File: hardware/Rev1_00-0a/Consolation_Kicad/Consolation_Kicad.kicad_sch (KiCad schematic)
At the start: 17 parts

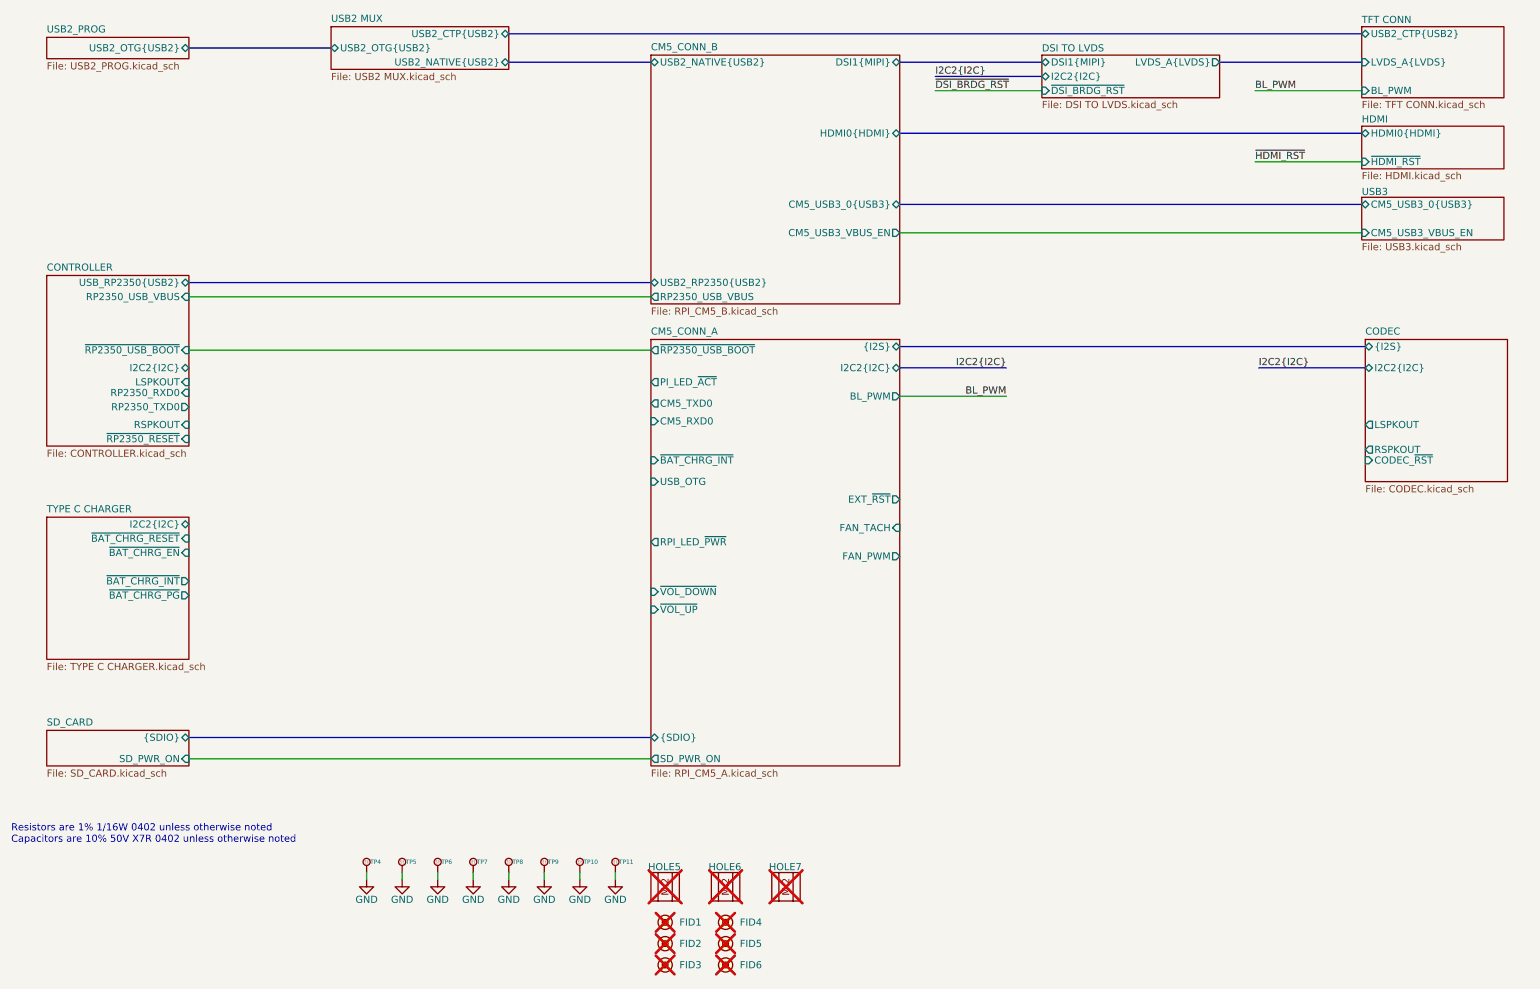
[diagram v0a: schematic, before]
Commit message: Major update to consolation schematics to include - Power supply - RESET SUPERVISOR - Review of GPIO and pinmux
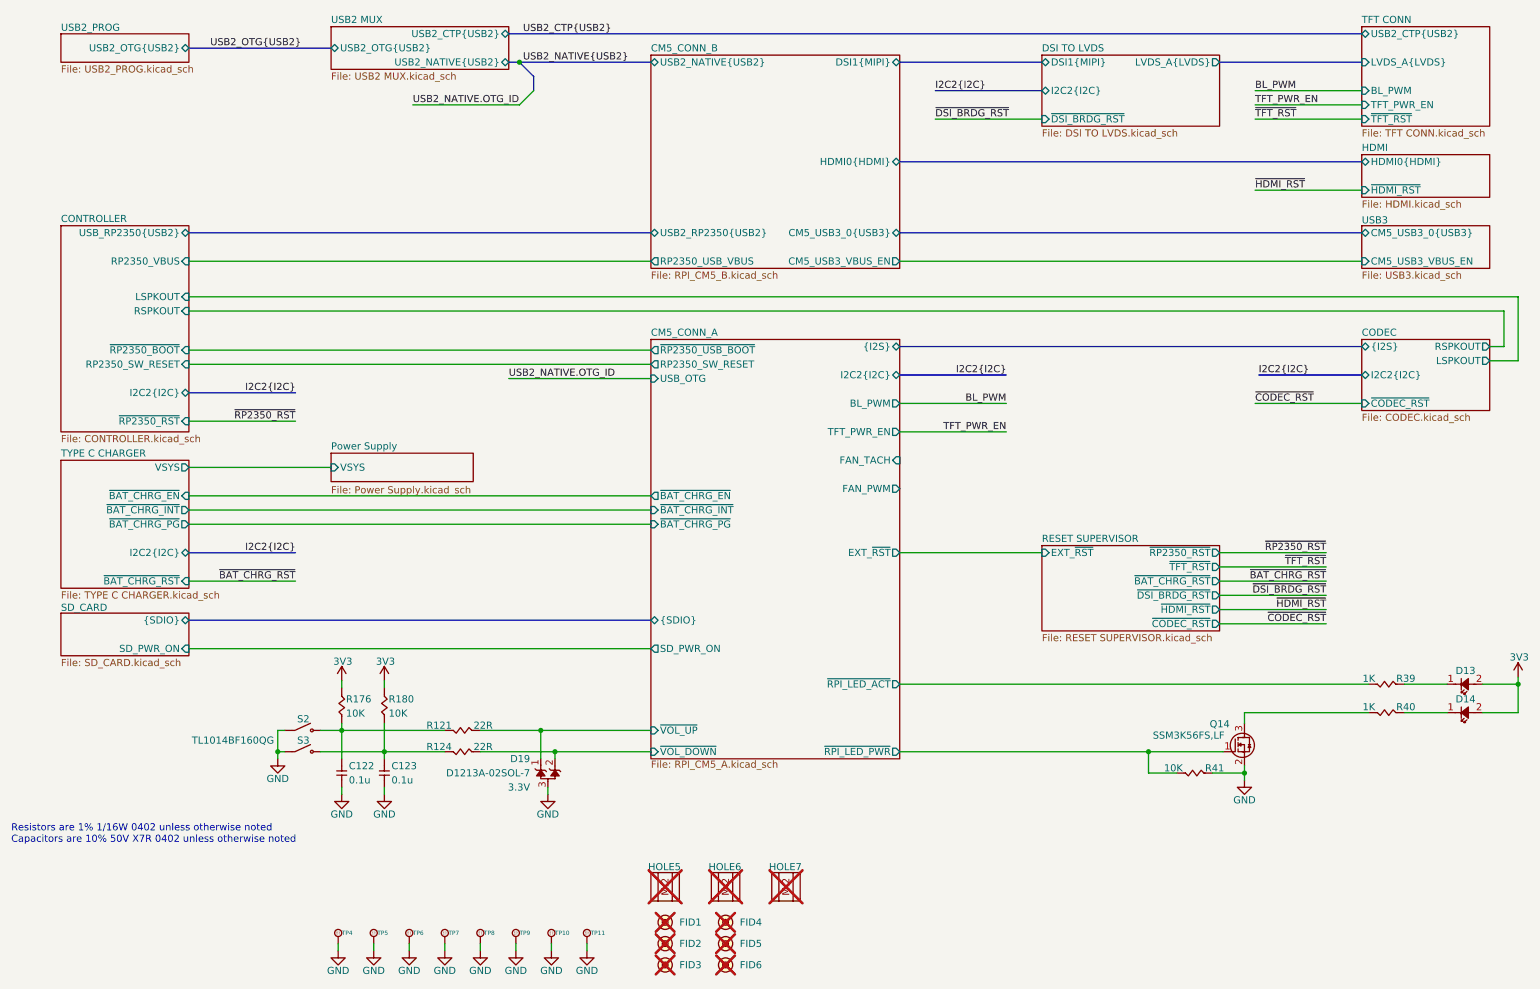
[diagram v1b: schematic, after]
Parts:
- added C122, C123: 0.1u, footprint:CAP_NONPOL_0402, symbol KicadCompDb:Capacitors/CAP_CER_SMT_00001
- added D13, D14: LTST-C190KGKT, footprint:LED_0603, symbol KicadCompDb:Diodes/DIODE_00007
- added D19: D1213A-02SOL-7, footprint:SOT-23-3, symbol KicadCompDb:ESD Diodes/ESD_DIODE_00002
- added Q14: SSM3K56FS,LF, footprint:SC-75, symbol KicadCompDb:Mosfet/MOSFET_00002
- added R121, R124: 22R, footprint:RES_0402, symbol KicadCompDb:Resistors/RES_SMT_00015
- added R176, R180, R41: 10K, footprint:RES_0402, symbol KicadCompDb:Resistors/RES_SMT_00013
- added R39, R40: 1K, footprint:RES_0402, symbol KicadCompDb:Resistors/RES_SMT_00004
- added S2, S3: TL1014BF160QG, footprint:TL1014B, symbol KicadCompDb:Miscellaneous/MISC_00016
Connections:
- net CM5_CONN_A/~{VOL_DOWN}: now also D19.2 (A), R124.1
- net CM5_CONN_A/~{VOL_UP}: now also D19.1, R121.1
- net GND: now also C122.1, C123.1, D19.3 (GND), Q14.2 (S), R41.2, S2.1, S3.1
- new net: C122.2, R121.2, R176.1, S2.2
- new net: Q14.3 (D), R40.2
- new net: D14.1 (K), R40.1
- new net: C123.2, R124.2, R180.1, S3.2
- new net: D13.1 (K), R39.1
- new net 3V3: D13.2 (A), D14.2 (A), R176.2, R180.2
- new net CM5_CONN_A/~{RPI_LED_ACT}: R39.2
- new net CM5_CONN_A/~{RPI_LED_PWR}: Q14.1 (G), R41.1
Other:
- added sheet Power Supply (Power Supply.kicad_sch)
- added sheet RESET SUPERVISOR (RESET SUPERVISOR.kicad_sch)
- sheet CM5_CONN_A ports: added RP2350_SW_RESET, TFT_PWR_EN, ~{BAT_CHRG_EN}, ~{BAT_CHRG_PG}, ~{RPI_LED_ACT}, ~{RPI_LED_PWR}; removed CM5_RXD0, CM5_TXD0, PI_LED_~{ACT}, RPI_LED_~{PWR}
- sheet CODEC ports: added ~{CODEC_RST}; removed CODEC_~{RST}
- sheet CONTROLLER ports: added RP2350_SW_RESET, RP2350_VBUS, ~{RP2350_BOOT}, ~{RP2350_RST}; removed RP2350_RXD0, RP2350_TXD0, RP2350_USB_VBUS, ~{RP2350_RESET}, ~{RP2350_USB_BOOT}
- sheet TFT CONN ports: added TFT_PWR_EN, ~{TFT_RST}; removed none
- sheet TYPE C CHARGER ports: added VSYS, ~{BAT_CHRG_RST}; removed ~{BAT_CHRG_RESET}
- moved on the sheet: TP10, TP11, TP4, TP5, TP6, TP7, TP8, TP9

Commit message: Removed unnecessary functions (USB2 mux, CapTouch) Adjusted 220uF alum capacitor for codec (slimmer version)
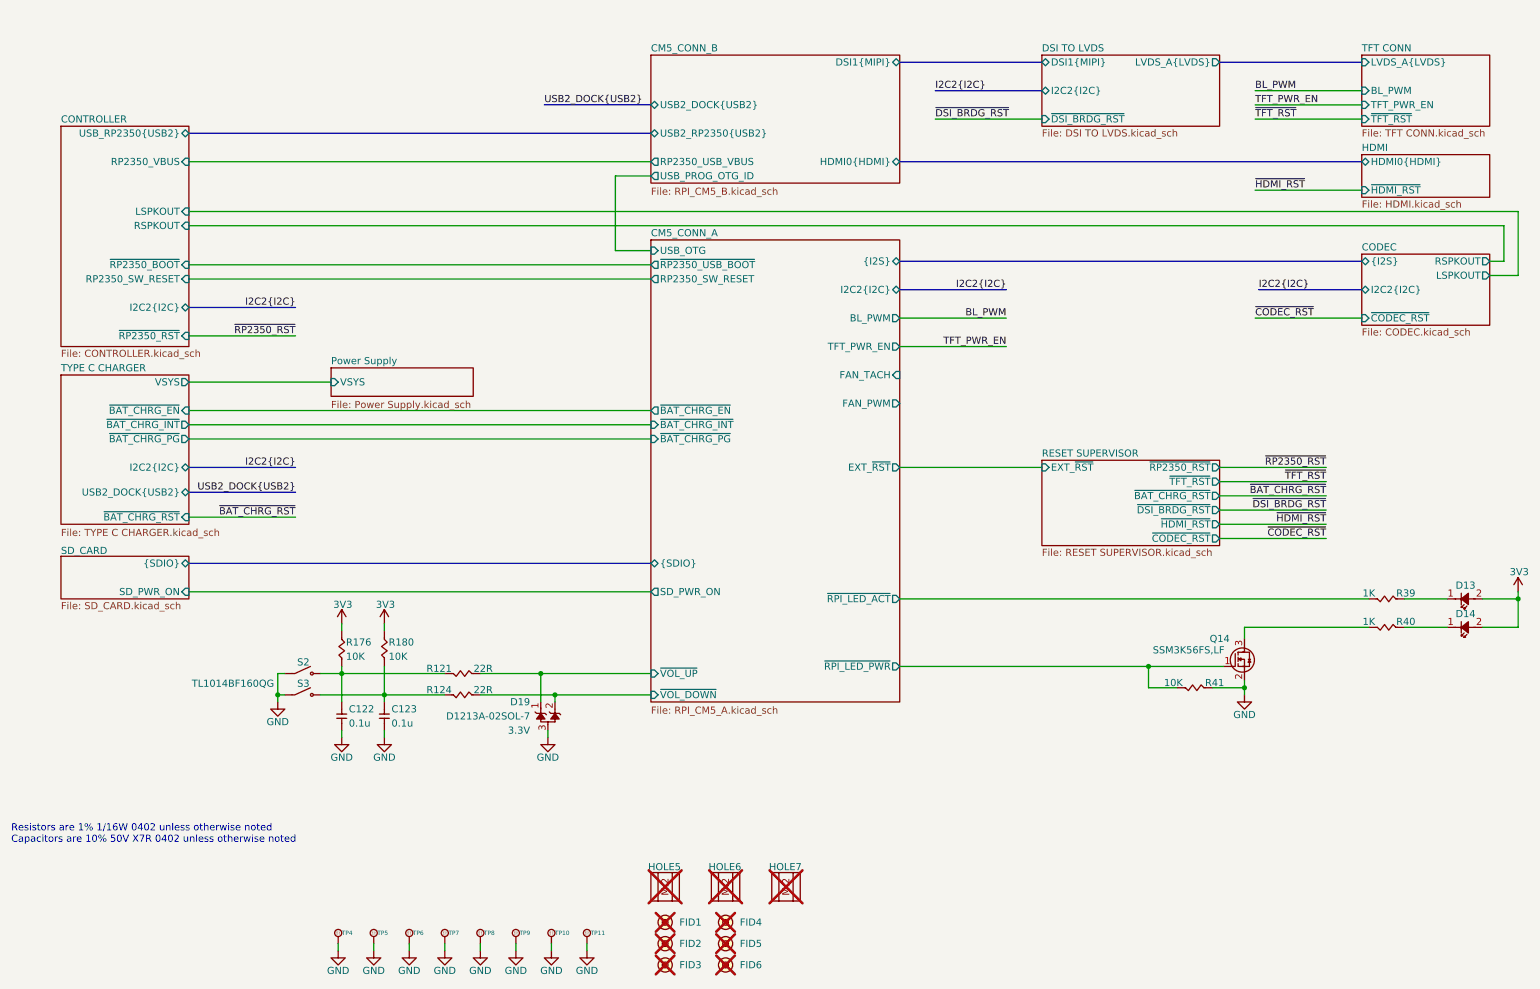
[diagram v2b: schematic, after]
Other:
- removed sheet USB2 MUX
- removed sheet USB2_PROG
- removed sheet USB3
- sheet CM5_CONN_B ports: added USB2_DOCK{USB2}, USB_PROG_OTG_ID; removed CM5_USB3_0{USB3}, CM5_USB3_VBUS_EN, USB2_NATIVE{USB2}
- sheet TFT CONN ports: added none; removed USB2_CTP{USB2}
- sheet TYPE C CHARGER ports: added USB2_DOCK{USB2}; removed none
- moved on the sheet: C122, C123, D13, D14, D19, Q14, R121, R124, R176, R180, R39, R40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

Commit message: Component preliminary placement
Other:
- sheet CM5_CONN_A ports: added none; removed TFT_PWR_EN
- sheet TFT CONN ports: added none; removed TFT_PWR_EN
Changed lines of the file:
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@@
 	(wire
 		(pts
-			(xy 234.95 40.64) (xy 254 40.64)
-		)
-		(stroke
-			(width 0)
-			(type default)
-		)
-	)
-	(wire
-		(pts
 			(xy 229.235 140.97) (xy 215.9 140.97)
 		)
@@
 	(wire
 		(pts
-			(xy 171.45 83.82) (xy 190.5 83.82)
-		)
-		(stroke
-			(width 0)
-			(type default)
-		)
-	)
-	(wire
-		(pts
 			(xy 255.27 133.985) (xy 233.045 133.985)
 		)
@@
 	(wire
 		(pts
-			(xy 234.95 38.1) (xy 254 38.1)
+			(xy 234.95 40.64) (xy 254 40.64)
 		)
 		(stroke
@@
 		)
 	)
-	(label "TFT_PWR_EN"
-		(at 190.5 83.82 180)
-		(effects
-			(font
-				(size 1.27 1.27)
-			)
-			(justify right bottom)
-		)
-	)
 	(label "~{RP2350_RST}"
 		(at 247.65 105.41 180)
@@
 	)
 	(label "BL_PWM"
-		(at 234.95 38.1 0)
+		(at 234.95 40.64 0)
 		(effects
 			(font
@@
 		)
 	)
-	(label "TFT_PWR_EN"
-		(at 234.95 40.64 0)
-		(effects
-			(font
-				(size 1.27 1.27)
-			)
-			(justify left bottom)
-		)
-	)
 	(label "~{HDMI_RST}"
 		(at 234.95 55.88 0)
@@
 			)
 		)
-		(pin "TFT_PWR_EN" output
-			(at 171.45 83.82 0)
-			(effects
-				(font
-					(size 1.27 1.27)
-				)
-				(justify right)
-			)
-		)
 		(pin "~{BAT_CHRG_EN}" output
 			(at 127 95.25 180)
@@
 		)
 		(pin "BL_PWM" input
-			(at 254 38.1 180)
+			(at 254 40.64 180)
 			(effects
 				(font
@@
 			(effects
 				(font
-					(size 1.27 1.27)
-				)
-				(justify left)
-			)
-		)
-		(pin "TFT_PWR_EN" input
-			(at 254 40.64 180)
-			(effects
-				(font

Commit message: Preliminary placement of Consolation continues
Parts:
- removed D19: D1213A-02SOL-7, footprint:SOT-23-3, symbol KicadCompDb:ESD Diodes/ESD_DIODE_00002
- added D1, D19: ESD7351HT1G, footprint:SOD-323, symbol KicadCompDb:ESD Diodes/ESD_DIODE_00006
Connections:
- net GND: now also D1.2 (A), D19.2 (A)
- net at C122.2, R121.2, R176.1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: now also D19.1 (K)
- net at C123.2, R124.2, R180.1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: now also D1.1 (K)

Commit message: Work on preliminary placement + RP2350A fanout
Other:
- sheet CM5_CONN_B ports: added RP2350_VBUS; removed RP2350_USB_VBUS
- sheet CONTROLLER ports: added USB2_RP2350{USB2}; removed USB_RP2350{USB2}
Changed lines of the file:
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@@
-			)
-		)
-		(pin "USB_RP2350{USB2}" bidirectional
-			(at 44.45 45.72 0)
-			(effects
-				(font
-					(size 1.27 1.27)
-				)
-				(justify right)
 			)
 		)
@@
 		(pin "RP2350_SW_RESET" input
 			(at 44.45 71.755 0)
+			(effects
+				(font
+					(size 1.27 1.27)
+				)
+				(justify right)
+			)
+		)
+		(pin "USB2_RP2350{USB2}" bidirectional
+			(at 44.45 45.72 0)
 			(effects
 				(font
@@
 			)
 		)
-		(pin "RP2350_USB_VBUS" output
-			(at 127 50.8 180)
-			(effects
-				(font
-					(size 1.27 1.27)
-				)
-				(justify left)
-			)
-		)
 		(pin "USB_PROG_OTG_ID" output
 			(at 127 53.34 180)
@@
 			(effects
 				(font
+					(size 1.27 1.27)
+				)
+				(justify left)
+			)
+		)
+		(pin "RP2350_VBUS" output
+			(at 127 50.8 180)
+			(effects
+				(font

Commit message: Continue preliminary placement To do : Power supplies + Type C charger
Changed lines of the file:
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@@
 	(title_block
 		(title "Consolation [Console Emulation]")
-		(date "2026-08-23")
+		(date "2026-08-29")
 		(rev "1.00-0A")
 		(comment 1 "Jean-Francois Bilodeau")
@@
 		(dnp no)
 		(property "Reference" "D14"
-			(at 272.542 131.572 0)
+			(at 272.542 131.826 0)
 			(show_name no)
 			(do_not_autoplace no)

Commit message: Preliminary placement done Add test points to PCB
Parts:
- removed TP10, TP11, TP4, TP5, TP6, TP7, TP8, TP9: (no value), symbol KiCad_Lib_Symbols:SMT_TP_100_MILS
- added TP1, TP2, TP24, TP25, TP3, TP4, TP5, TP6, TP7, TP8: 75 mils, footprint:SMT_TP_75_MILS, symbol KicadCompDb:Test Point/TP_00004
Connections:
- net GND: now also TP1.1, TP2.1, TP3.1, TP4.1, TP5.1, TP6.1, TP7.1, TP8.1
- net at C122.2, D19.1 (K), R121.2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: now also TP24.1
- net at C123.2, D1.1 (K), R124.2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: now also TP25.1
